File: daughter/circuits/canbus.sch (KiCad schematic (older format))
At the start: 10 parts, among them U15 MCP2551-I_SN

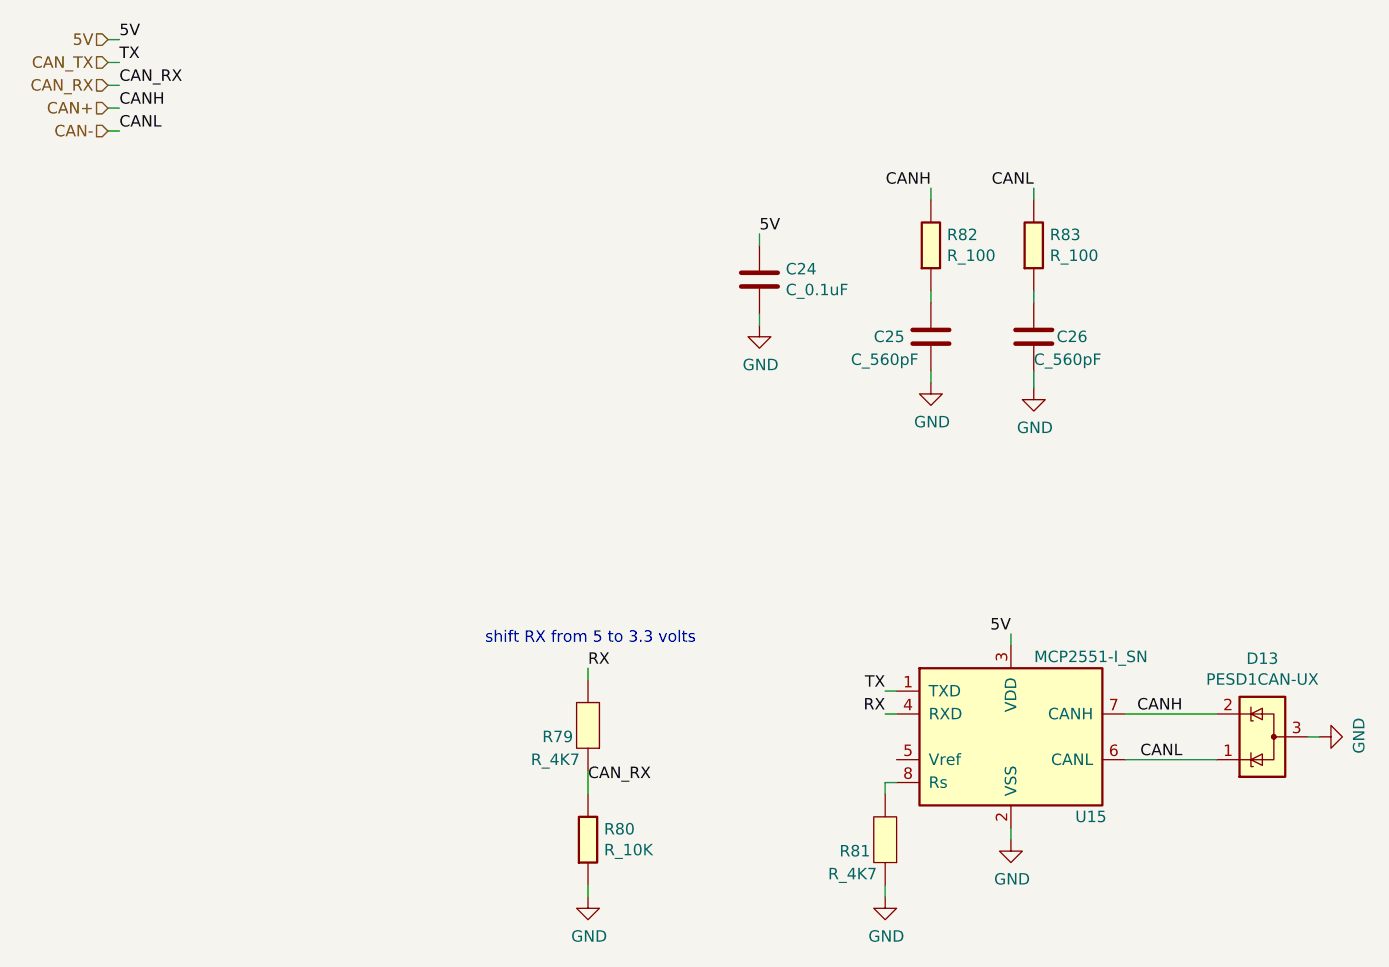
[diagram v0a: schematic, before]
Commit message: 0) Switched to h-bridge drivers for hvac 1) Connected ignition sense io 2) MCP config pins and reset 3) Fixed usb resistors 4) Fixed BJT footprint 5) Added car interface pcb for C6 Corvette
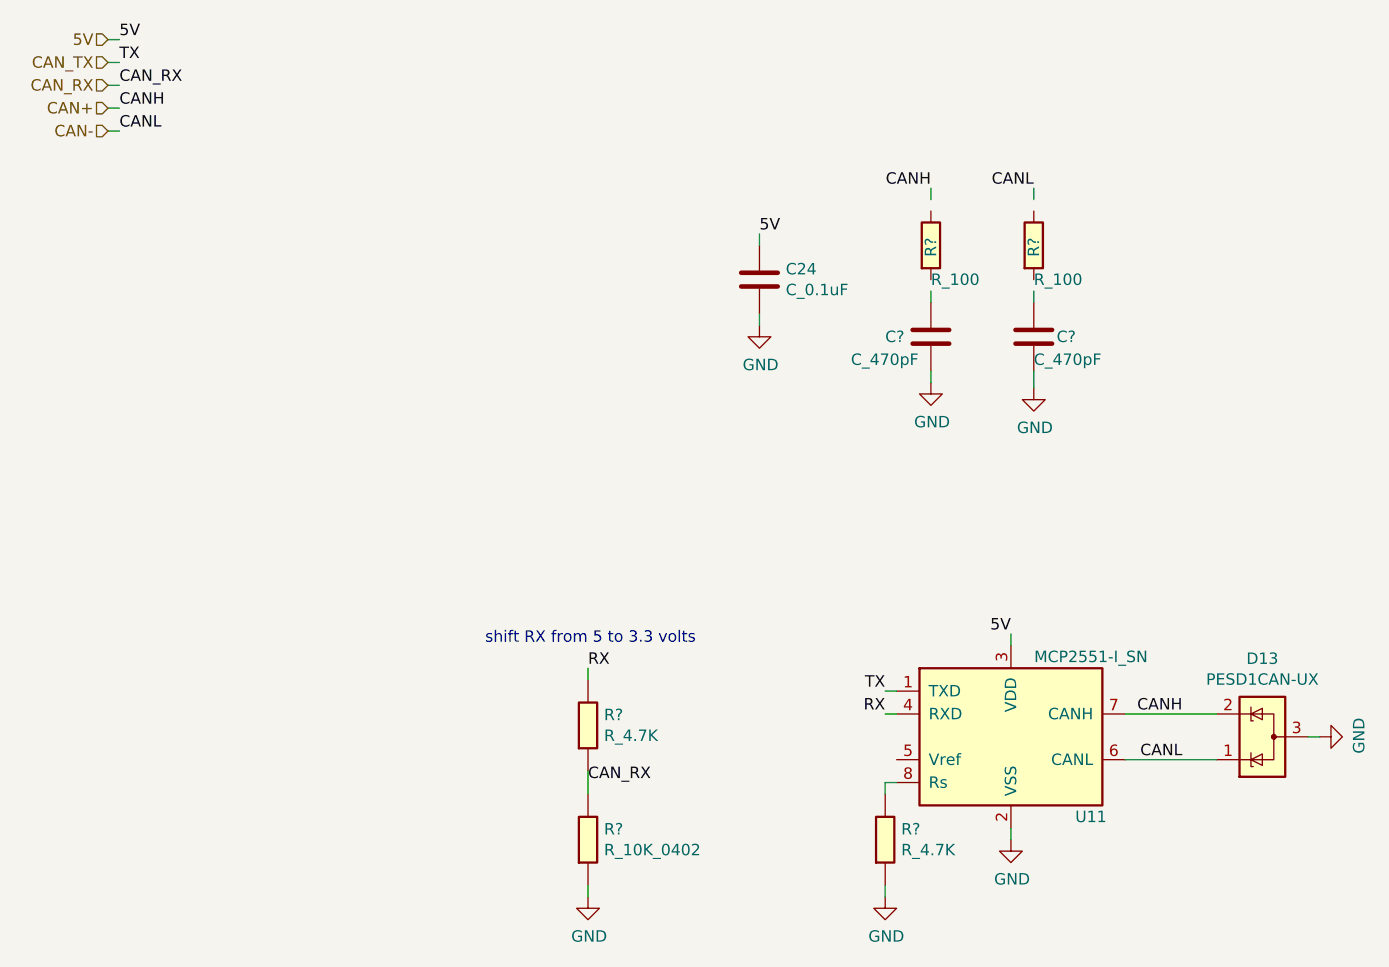
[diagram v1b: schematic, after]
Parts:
- removed C25, C26: C_560pF, Capacitor_SMD:C_0603_1608Metric_Pad1.08x0.95mm_HandSolder, symbol open-dash-daughterboard-rescue:C_560pF-Open_Automation
- removed R79, R81: R_4K7, Resistor_SMD:R_0603_1608Metric_Pad0.98x0.95mm_HandSolder, symbol open-dash-daughterboard-rescue:R_4K7-Open_Automation
- removed R80: R_10K, Resistor_SMD:R_0603_1608Metric_Pad0.98x0.95mm_HandSolder, symbol open-dash-daughterboard-rescue:R_10K-Open_Automation
- removed R82, R83: R_100, Resistor_SMD:R_0603_1608Metric_Pad0.98x0.95mm_HandSolder, symbol open-dash-daughterboard-rescue:R_100-Open_Automation
- added C? (x2): C_470pF, Capacitor_SMD:C_0603_1608Metric_Pad1.08x0.95mm_HandSolder, symbol Open_Automation:C_470pF
- added R? (x2): R_100, Resistor_SMD:R_0402_1005Metric_Pad0.72x0.64mm_HandSolder, symbol Open_Automation:R_100
- added R?: R_10K_0402, Resistor_SMD:R_0402_1005Metric_Pad0.72x0.64mm_HandSolder, symbol Open_Automation:R_10K_0402
- added R? (x2): R_4.7K, Resistor_SMD:R_0402_1005Metric_Pad0.72x0.64mm_HandSolder, symbol Open_Automation:R_4.7K
- renumbered U15 to U11

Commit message: finished schematic, working on layout
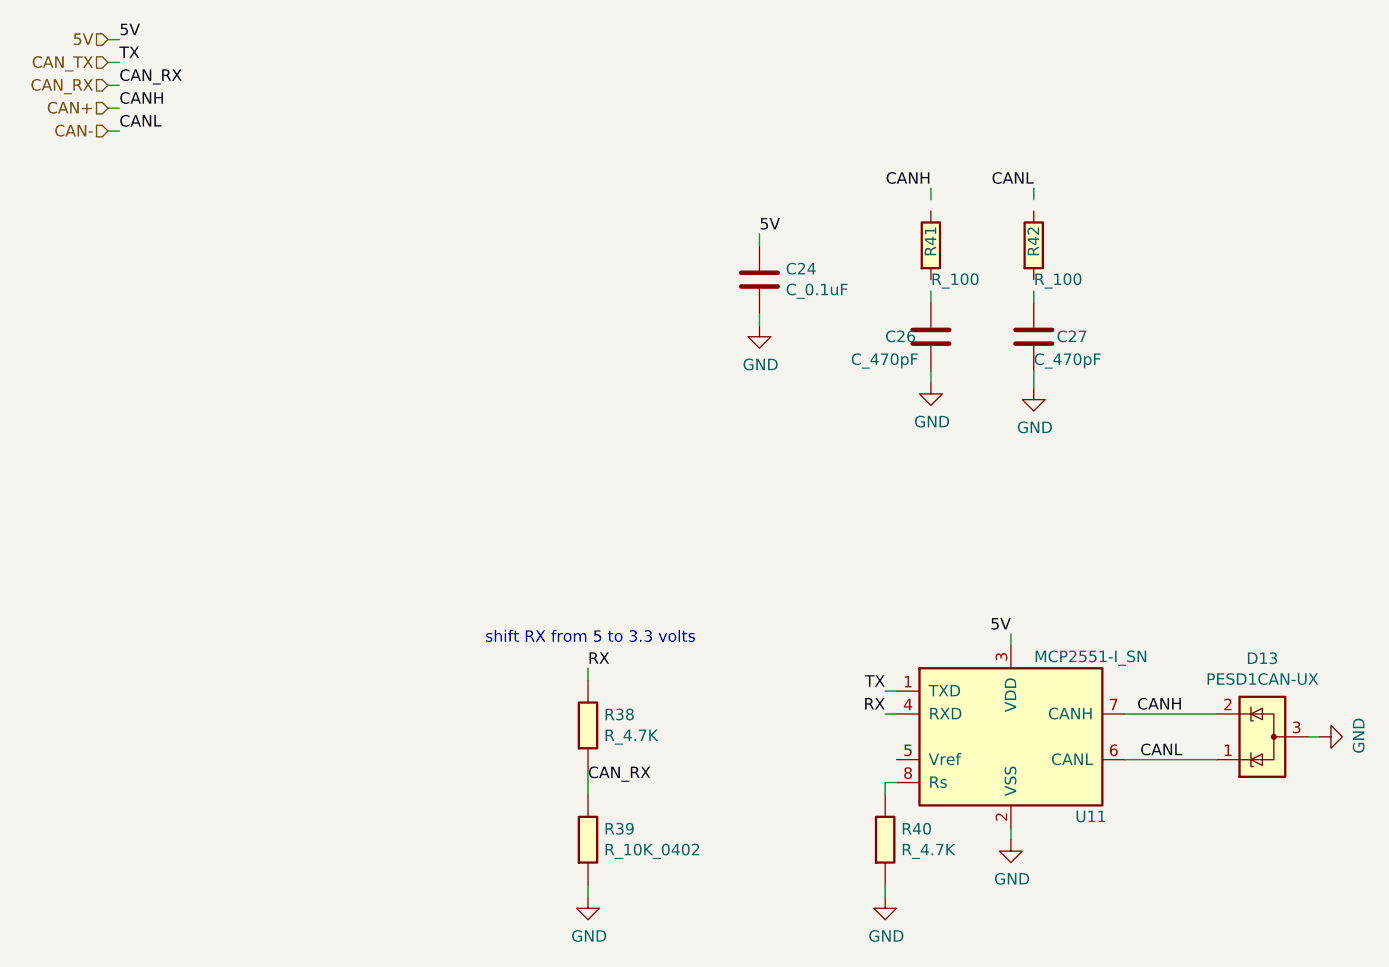
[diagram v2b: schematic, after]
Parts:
- gave numbers to parts that had none: 7
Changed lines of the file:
@@
 shift RX from 5 to 3.3 volts
 $Comp
-L Open_Automation:R_10K_0402 R?
+L Open_Automation:R_10K_0402 R39
 U 1 1 605738FD
 P 3600 4500
-F 0 "R?" H 3670 4546 50  0000 L CNN
+F 0 "R39" H 3670 4546 50  0000 L CNN
 F 1 "R_10K_0402" H 3670 4455 50  0000 L CNN
 F 2 "Resistor_SMD:R_0402_1005Metric_Pad0.72x0.64mm_HandSolder" V 3530 4500 50  0001 C CNN
@@
 $EndComp
 $Comp
-L Open_Automation:R_4.7K R?
+L Open_Automation:R_4.7K R38
 U 1 1 6057A3E4
 P 3600 4000
-F 0 "R?" H 3670 4046 50  0000 L CNN
+F 0 "R38" H 3670 4046 50  0000 L CNN
 F 1 "R_4.7K" H 3670 3955 50  0000 L CNN
 F 2 "Resistor_SMD:R_0402_1005Metric_Pad0.72x0.64mm_HandSolder" V 3530 4000 50  0001 C CNN
@@
 $EndComp
 $Comp
-L Open_Automation:R_4.7K R?
+L Open_Automation:R_4.7K R40
 U 1 1 6057D4BE
 P 4900 4500
-F 0 "R?" H 4970 4546 50  0000 L CNN
+F 0 "R40" H 4970 4546 50  0000 L CNN
 F 1 "R_4.7K" H 4970 4455 50  0000 L CNN
 F 2 "Resistor_SMD:R_0402_1005Metric_Pad0.72x0.64mm_HandSolder" V 4830 4500 50  0001 C CNN
@@
 $EndComp
 $Comp
-L Open_Automation:C_470pF C?
+L Open_Automation:C_470pF C27
 U 1 1 6047599C
 P 5550 2300
-F 0 "C?" H 5650 2300 50  0000 L CNN
+F 0 "C27" H 5650 2300 50  0000 L CNN
 F 1 "C_470pF" H 5550 2200 50  0000 L CNN
 F 2 "Capacitor_SMD:C_0603_1608Metric_Pad1.08x0.95mm_HandSolder" H 5650 2600 50  0001 C CNN
@@
 $EndComp
 $Comp
-L Open_Automation:C_470pF C?
+L Open_Automation:C_470pF C26
 U 1 1 604775F0
 P 5100 2300
-F 0 "C?" H 4900 2300 50  0000 L CNN
+F 0 "C26" H 4900 2300 50  0000 L CNN
 F 1 "C_470pF" H 4750 2200 50  0000 L CNN
 F 2 "Capacitor_SMD:C_0603_1608Metric_Pad1.08x0.95mm_HandSolder" H 5200 2600 50  0001 C CNN
@@
 $EndComp
 $Comp
-L Open_Automation:R_100 R?
+L Open_Automation:R_100 R41
 U 1 1 604944AE
 P 5100 1900
-F 0 "R?" V 5100 1850 50  0000 L CNN
+F 0 "R41" V 5100 1850 50  0000 L CNN
 F 1 "R_100" H 5100 1750 50  0000 L CNN
 F 2 "Resistor_SMD:R_0402_1005Metric_Pad0.72x0.64mm_HandSolder" V 5030 1900 50  0001 C CNN
@@
 $EndComp
 $Comp
-L Open_Automation:R_100 R?
+L Open_Automation:R_100 R42
 U 1 1 60494C03
 P 5550 1900
-F 0 "R?" V 5550 1850 50  0000 L CNN
+F 0 "R42" V 5550 1850 50  0000 L CNN
 F 1 "R_100" H 5550 1750 50  0000 L CNN
 F 2 "Resistor_SMD:R_0402_1005Metric_Pad0.72x0.64mm_HandSolder" V 5480 1900 50  0001 C CNN

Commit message: sent v1.2 to fab
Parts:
- removed U11: MCP2551-I_SN, Package_SO:SOIC-8_3.9x4.9mm_P1.27mm, symbol open-dash-daughterboard-rescue:MCP2551-I-SN-Interface_CAN_LIN
- added U3: CAN_MCP2551-I-SN, Package_SO:SOIC-8_3.9x4.9mm_P1.27mm, symbol Open_Automation:CAN_MCP2551-I-SN
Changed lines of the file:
@@
-$EndComp
-$Comp
-L open-dash-daughterboard-rescue:MCP2551-I-SN-Interface_CAN_LIN U?
-U 1 1 5AD6C5A2
-P 5450 4050
-AR Path="/5A8CA1AF/5AD6C5A2" Ref="U?"  Part="1"
-AR Path="/60D3331D/5AD6C5A2" Ref="U11"  Part="1"
-F 0 "U11" H 5800 3700 50  0000 C CNN
-F 1 "MCP2551-I_SN" H 5800 4400 50  0000 C CNN
-F 2 "Package_SO:SOIC-8_3.9x4.9mm_P1.27mm" H 5450 3550 50  0001 C CIN
-F 3 "https://datasheet.lcsc.com/szlcsc/Microchip-Tech-MCP2551-I-SN_C7376.pdf" H 5450 4050 50  0001 C CNN
-F 4 "MCP2551-I/SN" H 5450 4050 50  0001 C CNN "Part Number"
-F 5 "C7376" H 0   0   50  0001 C CNN "LCSC"
-	1    5450 4050
-	1    0    0    -1
 $EndComp
 $Comp
@@
 	1    0    0    -1
 $EndComp
+$Comp
+L Open_Automation:CAN_MCP2551-I-SN U3
+U 1 1 60714385
+P 5450 4050
+F 0 "U3" H 5100 4400 50  0000 C CNN
+F 1 "CAN_MCP2551-I-SN" H 5850 4400 50  0000 C CNN
+F 2 "Package_SO:SOIC-8_3.9x4.9mm_P1.27mm" H 5450 3550 50  0001 C CIN
+F 3 "https://datasheet.lcsc.com/szlcsc/Microchip-Tech-MCP2551-I-SN_C7376.pdf" H 5450 4050 50  0001 C CNN
+F 4 "MCP2551-I/SN" H 5850 4500 50  0001 C CNN "Part Number"
+F 5 "C7376" H 5800 4600 50  0001 C CNN "LCSC"
+	1    5450 4050
+	1    0    0    -1
+$EndComp

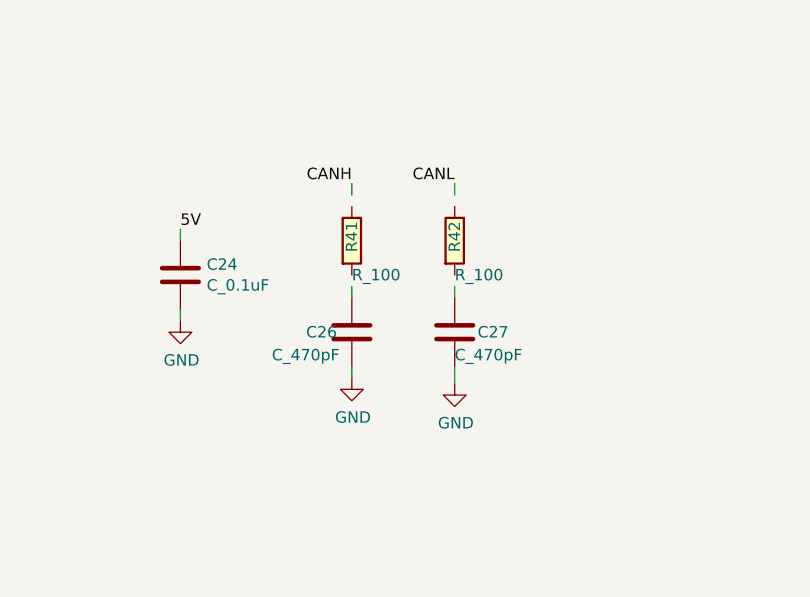
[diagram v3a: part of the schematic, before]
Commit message: Added external amp trigger code and circuit to PCB. Made some layout modifications.
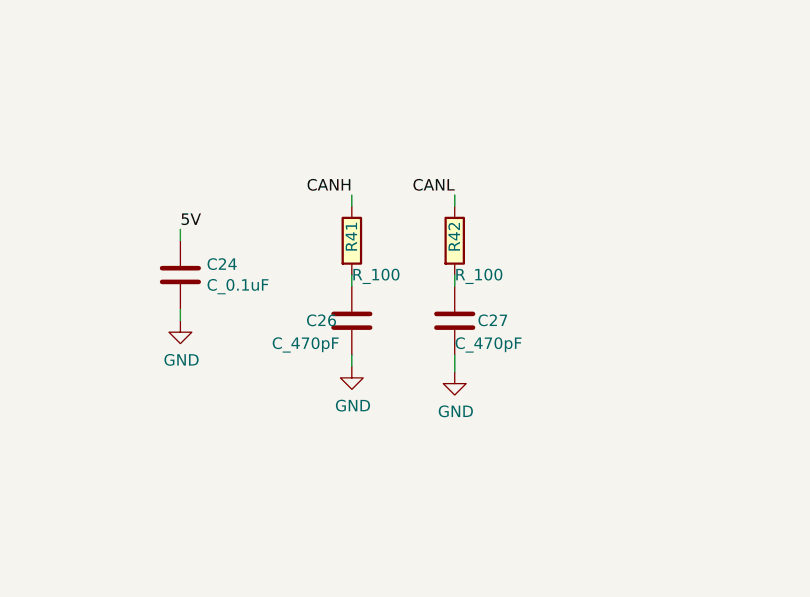
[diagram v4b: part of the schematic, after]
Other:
- moved on the sheet: C26, C27
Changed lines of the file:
@@
 5V
 Wire Wire Line
-	5550 2450 5550 2525
+	5550 2400 5550 2475
 Text HLabel 1500 1200 0    50   Input ~ 0
 CAN_RX
@@
 Text Label 6200 4150 2    50   ~ 0
 CANL
-Text Label 5100 1650 2    50   ~ 0
+Text Label 5100 1700 2    50   ~ 0
 CANH
 Wire Wire Line
-	5100 2500 5100 2450
+	5100 2450 5100 2400
 Wire Wire Line
 	6800 4050 6750 4050
 Wire Wire Line
-	5100 1650 5100 1700
-Text Label 5550 1650 2    50   ~ 0
+	5100 1700 5100 1750
+Text Label 5550 1700 2    50   ~ 0
 CANL
 Wire Wire Line
-	5550 1650 5550 1700
+	5550 1700 5550 1750
 Text Label 6200 3950 2    50   ~ 0
 CANH
@@
 	5450 4500 5450 4450
 Wire Wire Line
-	5550 2150 5550 2100
-Wire Wire Line
-	5100 2150 5100 2100
+	5550 2100 5550 2050
+Wire Wire Line
+	5100 2100 5100 2050
 $Comp
 L open-dash-daughterboard-rescue:GND-power #PWR?
@@
 L open-dash-daughterboard-rescue:GND-power #PWR?
 U 1 1 5ADD7680
-P 5550 2525
+P 5550 2475
 AR Path="/5A8CA1AF/5ADD7680" Ref="#PWR?"  Part="1"
 AR Path="/60D3331D/5ADD7680" Ref="#PWR086"  Part="1"
-F 0 "#PWR086" H 5550 2275 50  0001 C CNN
-F 1 "GND" H 5555 2352 50  0000 C CNN
-F 2 "" H 5550 2525 50  0001 C CNN
-F 3 "" H 5550 2525 50  0001 C CNN
-	1    5550 2525
+F 0 "#PWR086" H 5550 2225 50  0001 C CNN
+F 1 "GND" H 5555 2302 50  0000 C CNN
+F 2 "" H 5550 2475 50  0001 C CNN
+F 3 "" H 5550 2475 50  0001 C CNN
+	1    5550 2475
 	1    0    0    -1
 $EndComp
@@
 L open-dash-daughterboard-rescue:GND-power #PWR?
 U 1 1 5CC02094
-P 5100 2500
+P 5100 2450
 AR Path="/5A8CA1AF/5CC02094" Ref="#PWR?"  Part="1"
 AR Path="/60D3331D/5CC02094" Ref="#PWR084"  Part="1"
-F 0 "#PWR084" H 5100 2250 50  0001 C CNN
-F 1 "GND" H 5105 2327 50  0000 C CNN
-F 2 "" H 5100 2500 50  0001 C CNN
-F 3 "" H 5100 2500 50  0001 C CNN
-	1    5100 2500
+F 0 "#PWR084" H 5100 2200 50  0001 C CNN
+F 1 "GND" H 5105 2277 50  0000 C CNN
+F 2 "" H 5100 2450 50  0001 C CNN
+F 3 "" H 5100 2450 50  0001 C CNN
+	1    5100 2450
 	1    0    0    -1
 $EndComp
@@
 L Open_Automation:C_470pF C27
 U 1 1 6047599C
-P 5550 2300
-F 0 "C27" H 5650 2300 50  0000 L CNN
-F 1 "C_470pF" H 5550 2200 50  0000 L CNN
-F 2 "Capacitor_SMD:C_0603_1608Metric_Pad1.08x0.95mm_HandSolder" H 5650 2600 50  0001 C CNN
-F 3 "https://datasheet.lcsc.com/szlcsc/Guangdong-Fenghua-Advanced-Tech-0402B471K500NT_C1537.pdf" H 5550 2050 50  0001 C CNN
-F 4 "0402B471K500NT" H 5675 2500 60  0001 C CNN "Part Number"
-F 5 "C1537" H 5550 2700 50  0001 C CNN "LCSC"
-	1    5550 2300
+P 5550 2250
+F 0 "C27" H 5650 2250 50  0000 L CNN
+F 1 "C_470pF" H 5550 2150 50  0000 L CNN
+F 2 "Capacitor_SMD:C_0603_1608Metric_Pad1.08x0.95mm_HandSolder" H 5650 2550 50  0001 C CNN
+F 3 "https://datasheet.lcsc.com/szlcsc/Guangdong-Fenghua-Advanced-Tech-0402B471K500NT_C1537.pdf" H 5550 2000 50  0001 C CNN
+F 4 "0402B471K500NT" H 5675 2450 60  0001 C CNN "Part Number"
+F 5 "C1537" H 5550 2650 50  0001 C CNN "LCSC"
+	1    5550 2250
 	1    0    0    -1
 $EndComp
@@
 L Open_Automation:C_470pF C26
 U 1 1 604775F0
-P 5100 2300
-F 0 "C26" H 4900 2300 50  0000 L CNN
-F 1 "C_470pF" H 4750 2200 50  0000 L CNN
-F 2 "Capacitor_SMD:C_0603_1608Metric_Pad1.08x0.95mm_HandSolder" H 5200 2600 50  0001 C CNN
-F 3 "https://datasheet.lcsc.com/szlcsc/Guangdong-Fenghua-Advanced-Tech-0402B471K500NT_C1537.pdf" H 5100 2050 50  0001 C CNN
-F 4 "0402B471K500NT" H 5225 2500 60  0001 C CNN "Part Number"
-F 5 "C1537" H 5100 2700 50  0001 C CNN "LCSC"
-	1    5100 2300
-	1    0    0    -1
-$EndComp
+P 5100 2250
+F 0 "C26" H 4900 2250 50  0000 L CNN
+F 1 "C_470pF" H 4750 2150 50  0000 L CNN
+F 2 "Capacitor_SMD:C_0603_1608Metric_Pad1.08x0.95mm_HandSolder" H 5200 2550 50  0001 C CNN
+F 3 "https://datasheet.lcsc.com/szlcsc/Guangdong-Fenghua-Advanced-Tech-0402B471K500NT_C1537.pdf" H 5100 2000 50  0001 C CNN
+F 4 "0402B471K500NT" H 5225 2450 60  0001 C CNN "Part Number"
+F 5 "C1537" H 5100 2650 50  0001 C CNN "LCSC"
+	1    5100 2250
+	1    0    0    -1
+$EndComp
